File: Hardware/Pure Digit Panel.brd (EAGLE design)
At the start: 20.3 x 128.4 mm, 0 parts

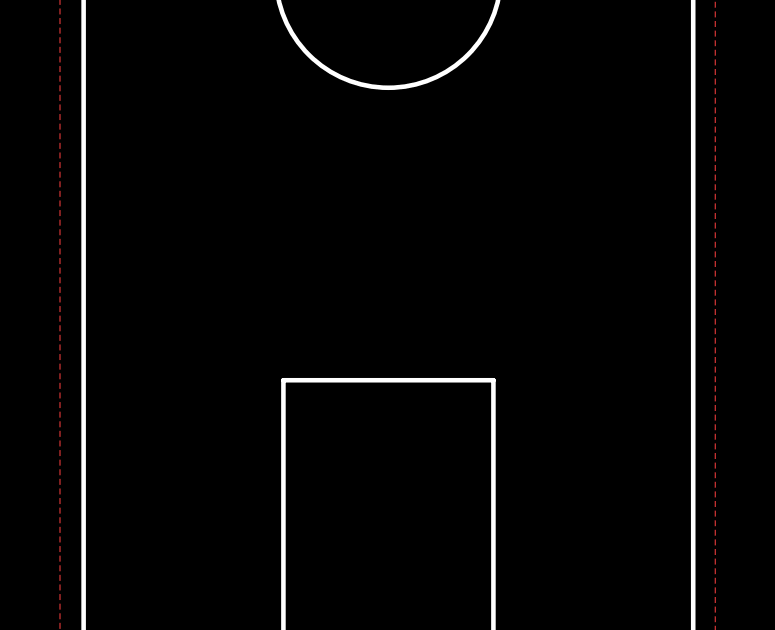
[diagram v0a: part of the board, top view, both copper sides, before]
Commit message: Digit 2.0
Digit Updated to V2.0 28/4/21

RC filter added to DAC output.
Cap added to output opamp.
SD Card Reader added.

To do: Replace power so 5V comes from case power supply, inline with low noise techniques. May require complete redesign.
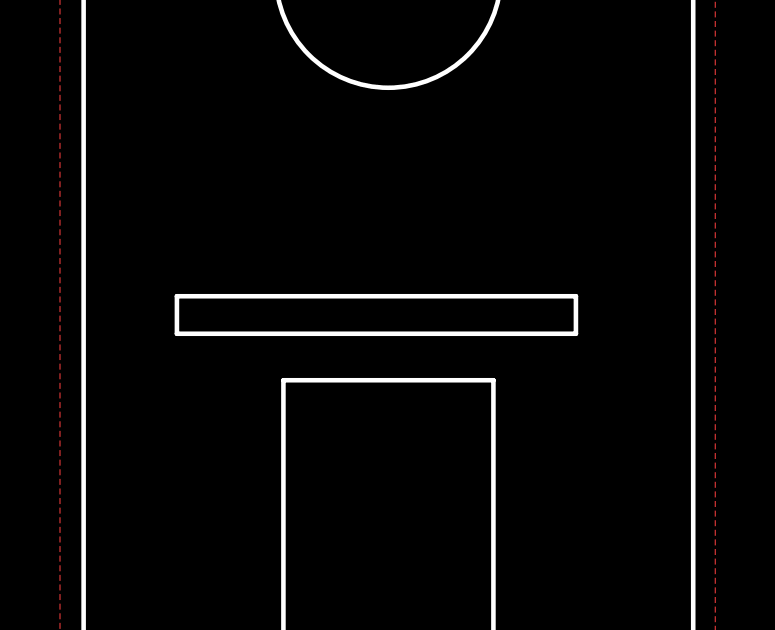
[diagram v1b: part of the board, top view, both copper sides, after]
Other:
- outline, holes or cut-outs redrawn
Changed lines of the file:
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@@
 <?xml version="1.0" encoding="utf-8"?>
 <!DOCTYPE eagle SYSTEM "eagle.dtd">
-<eagle version="9.2.0">
+<eagle version="9.6.2">
 <drawing>
 <settings>
-<setting alwaysvectorfont="yes"/>
+<setting alwaysvectorfont="no"/>
 <setting verticaltext="up"/>
 </settings>
@@
 <rectangle x1="2.1971" y1="122.5423" x2="5.8039" y2="122.5677" layer="29"/>
 <rectangle x1="2.2479" y1="122.5677" x2="5.7023" y2="122.5931" layer="29"/>
+<wire x1="3.11" y1="93.5" x2="16.41" y2="93.5" width="0.1524" layer="20"/>
+<wire x1="16.41" y1="93.5" x2="16.41" y2="92.25" width="0.1524" layer="20"/>
+<wire x1="16.41" y1="92.25" x2="3.11" y2="92.25" width="0.1524" layer="20"/>
+<wire x1="3.11" y1="92.25" x2="3.11" y2="93.5" width="0.1524" layer="20"/>
 </plain>
 <attributes>
